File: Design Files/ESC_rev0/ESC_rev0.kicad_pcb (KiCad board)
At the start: 2 copper layers, 176 parts, among them J1 Conn_01x08, J2 Conn_01x06, J3 Conn_01x03, J4 WP-BUTR, J5 WP-BUTR, J6 WP-BUTR, J7 Conn_01x04_Shielded, J8 Conn_01x06, J9 USB_C_Receptacle_USB2.0_16P, Q1 HSBA15810C, Q2 HSBA15810C, Q3 HSBA15810C, Q4 HSBA15810C, Q5 HSBA15810C, Q6 HSBA15810C, SW1 SW_DIP_x01, U1 XT30PW-M, U2 XH-2PWBPZ, U3 AMS1117-3.3, U4 STM32F405RGTx, U5 DRV8302DCA, U6 ESDCAN24-2BLY, U7 SN65HVD230, Y1 Crystal

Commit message: update 14
Circuits separated by schematic pages. Replaced crystal footprint.
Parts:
- Y1: footprint Crystal:Crystal_HC50_Vertical -> Crystal:Crystal_SMD_2012-2Pin_2.0x1.2mm_HandSoldering
- moved H1 104.5 mm to (161.9, 152.8)
- moved H4 104.5 mm to (161.9, 176.7)
- moved R61 104.5 mm to (167.9, 150.1)
- moved R64 104.5 mm to (167.9, 157.6)
- moved H2 104.5 mm to (161.9, 160.8)
- moved R62 104.5 mm to (167.9, 152.6)
- moved R63 104.5 mm to (167.9, 155.1)
- moved H3 104.5 mm to (161.9, 168.7)
- moved D1 104.3 mm to (76.1, 33.3), turned to -90 degrees
- moved U1 98.1 mm to (70.2, 31.0), turned to 90 degrees
- moved C4 87.7 mm to (84.2, 54.5), turned to 180 degrees
- moved C2 84.6 mm to (105.8, 37.1), turned to 90 degrees
- moved C3 83.7 mm to (86.4, 56.1)
- moved R2 83.3 mm to (85.0, 47.4)
- moved R3 83.3 mm to (85.0, 49.9)
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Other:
- board text added: "Analog"
- board text added: "CAN"
- board text added: "Digital"
- board text added: "Filters"
- board text added: "Input Protection"
- board text added: "MCU"
- board text added: "MOSFET Driver"
- board text added: "MOSFETs"
- board text added: "Mechanical"
- board text added: "Power"
- board text added: "Step Down"
- board text added: "USB"

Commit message: update 15
Simple connectors replaced by smd connectors (downloaded). Connectors were placed in edges of the board.
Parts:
- C1, C2: moved to B.Cu
- H1, H2, H3, H4: footprint MountingHole:MountingHole_3.2mm_M3 -> MountingHole:MountingHole_3.2mm_M3_Pad_Via
- J1: footprint Connector_PinHeader_2.00mm:PinHeader_1x08_P2.00mm_Vertical -> HX25003-8AWB:CONN-SMD_8P-P2.50_HX25003-8AWB
- J2, J8: footprint Connector_PinHeader_2.00mm:PinHeader_1x06_P2.00mm_Vertical -> S6B-XH-SM4-TB:CONN_S6B-XH-SM4-TB_JST
- J3: footprint Connector_PinHeader_2.00mm:PinHeader_1x03_P2.00mm_Vertical -> S3B-XH-SM4-TB:CONN3_S3B-XH_JST
- J7: value Conn_01x04_Shielded -> Conn_01x04; footprint Connector_PinHeader_2.00mm:PinHeader_1x04_P2.00mm_Vertical -> S4B-XH-SM4-TB:CONN4_S4B-XH_JST
- U1: value XT30PW-M -> XT60PW-M; footprint Connector_AMASS:AMASS_XT30PW-M_1x02_P2.50mm_Horizontal -> XT60PW-M:XT60PWM
- Y1: footprint Crystal:Crystal_SMD_2012-2Pin_2.0x1.2mm_HandSoldering -> Crystal:Crystal_SMD_0603-4Pin_6.0x3.5mm_HandSoldering
- moved J4 177.7 mm to (220.3, 49.9)
- moved J5 177.7 mm to (220.3, 63.0)
- moved J6 177.7 mm to (220.3, 76.0)
- moved CR1 177.7 mm to (48.0, 44.4)
- moved R54 177.7 mm to (44.1, 33.7)
- moved R55 177.7 mm to (44.1, 36.2)
- moved R56 177.7 mm to (44.1, 38.7)
- moved R57 177.7 mm to (44.1, 41.3)
- moved R58 177.7 mm to (44.1, 43.8)
- moved R59 177.7 mm to (44.1, 46.3)
- moved R60 177.7 mm to (44.1, 48.8)
- moved R33 166.1 mm to (245.0, 108.9)
- moved R34 166.1 mm to (245.0, 111.4)
- moved R35 166.1 mm to (245.0, 113.9)
- moved R36 166.1 mm to (245.0, 116.4)
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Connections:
- J1 pad 1: /MCU/+5V_COM -> GND
- J1 pad 2: /MCU/+3V3_COM -> /MCU/MISO_ADC_EXT2
- J1 pad 3: GND -> /MCU/RX_SCL_MOSI
- J1 pad 4: /MCU/SCK_ADC_EXT -> /MCU/TX_SDA_NSS
- J1 pad 5: /MCU/TX_SDA_NSS -> /MCU/SCK_ADC_EXT
- J1 pad 6: /MCU/RX_SCL_MOSI -> GND
- J1 pad 7: /MCU/MISO_ADC_EXT2 -> /MCU/+3V3_COM
- J1 pad 8: GND -> /MCU/+5V_COM
- U1 pad 1: GND -> +VDC
- U1 pad 2: +VDC -> GND
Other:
- board outline added: 100 x 75 mm
- copper layers 2 -> 4
- board text added: "COM"
- board text added: "Prog"
- board text added: "Sensors"
- board text added: "Servo"
- board text removed: "Mechanical"

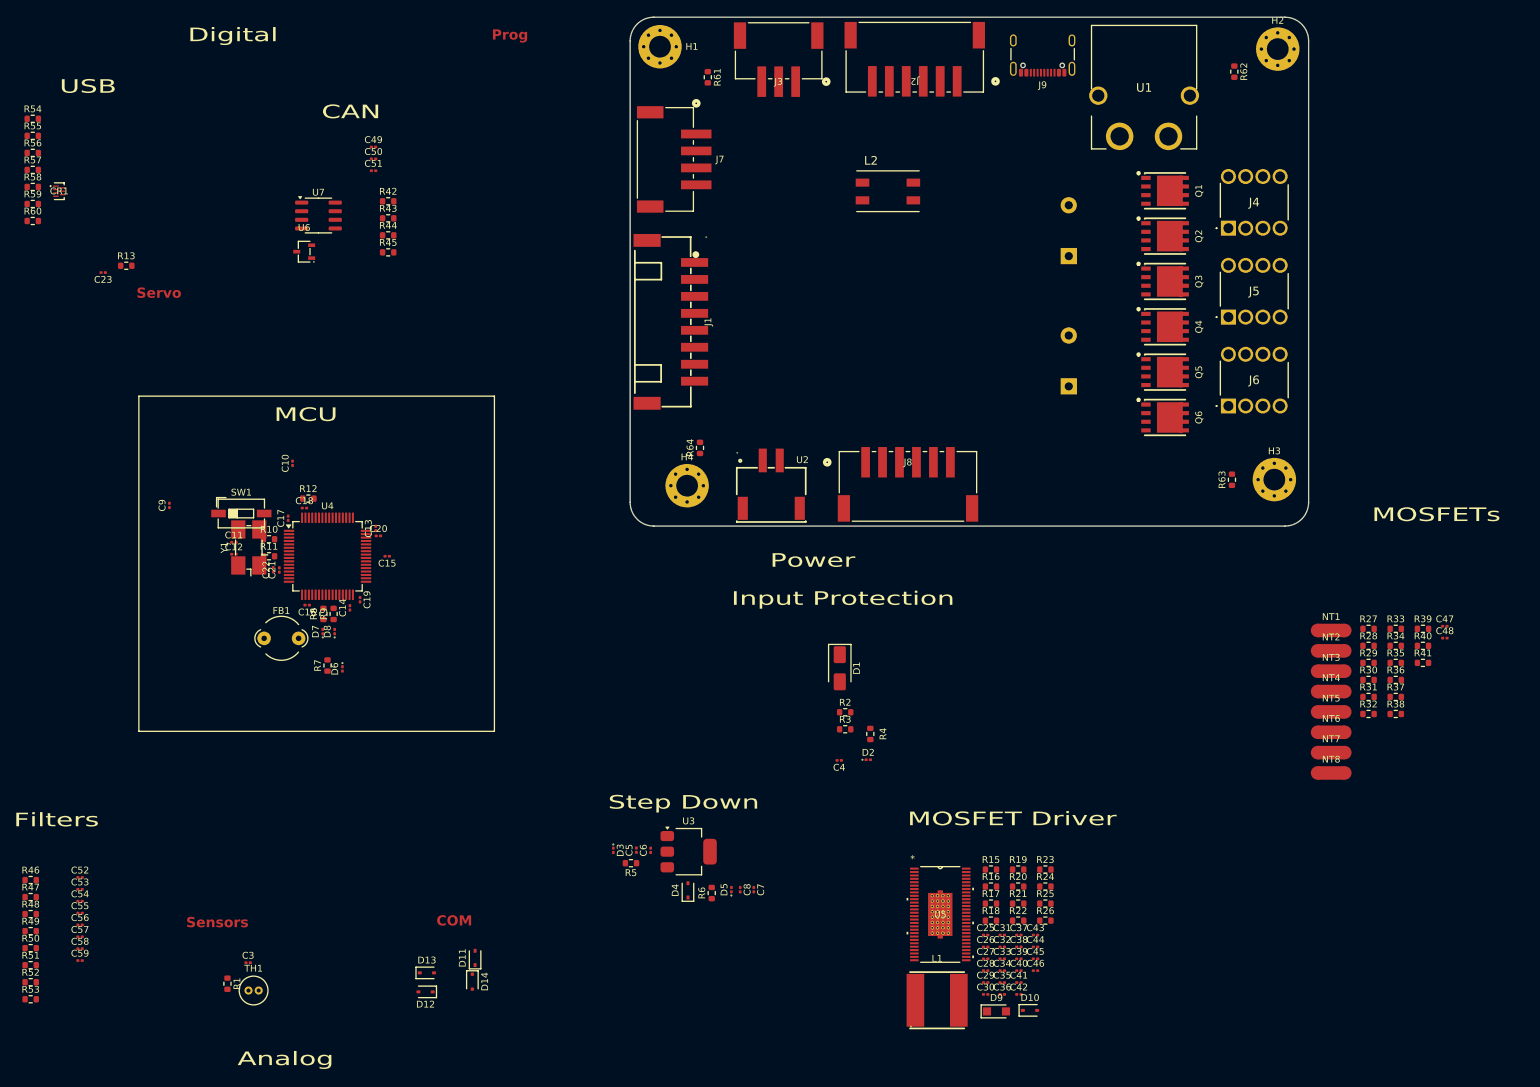
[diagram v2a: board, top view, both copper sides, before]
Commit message: update 16
All components placed on board. Some components modifications and addition were made: added 3D models, changed some symbols and footprints positions and some component types.
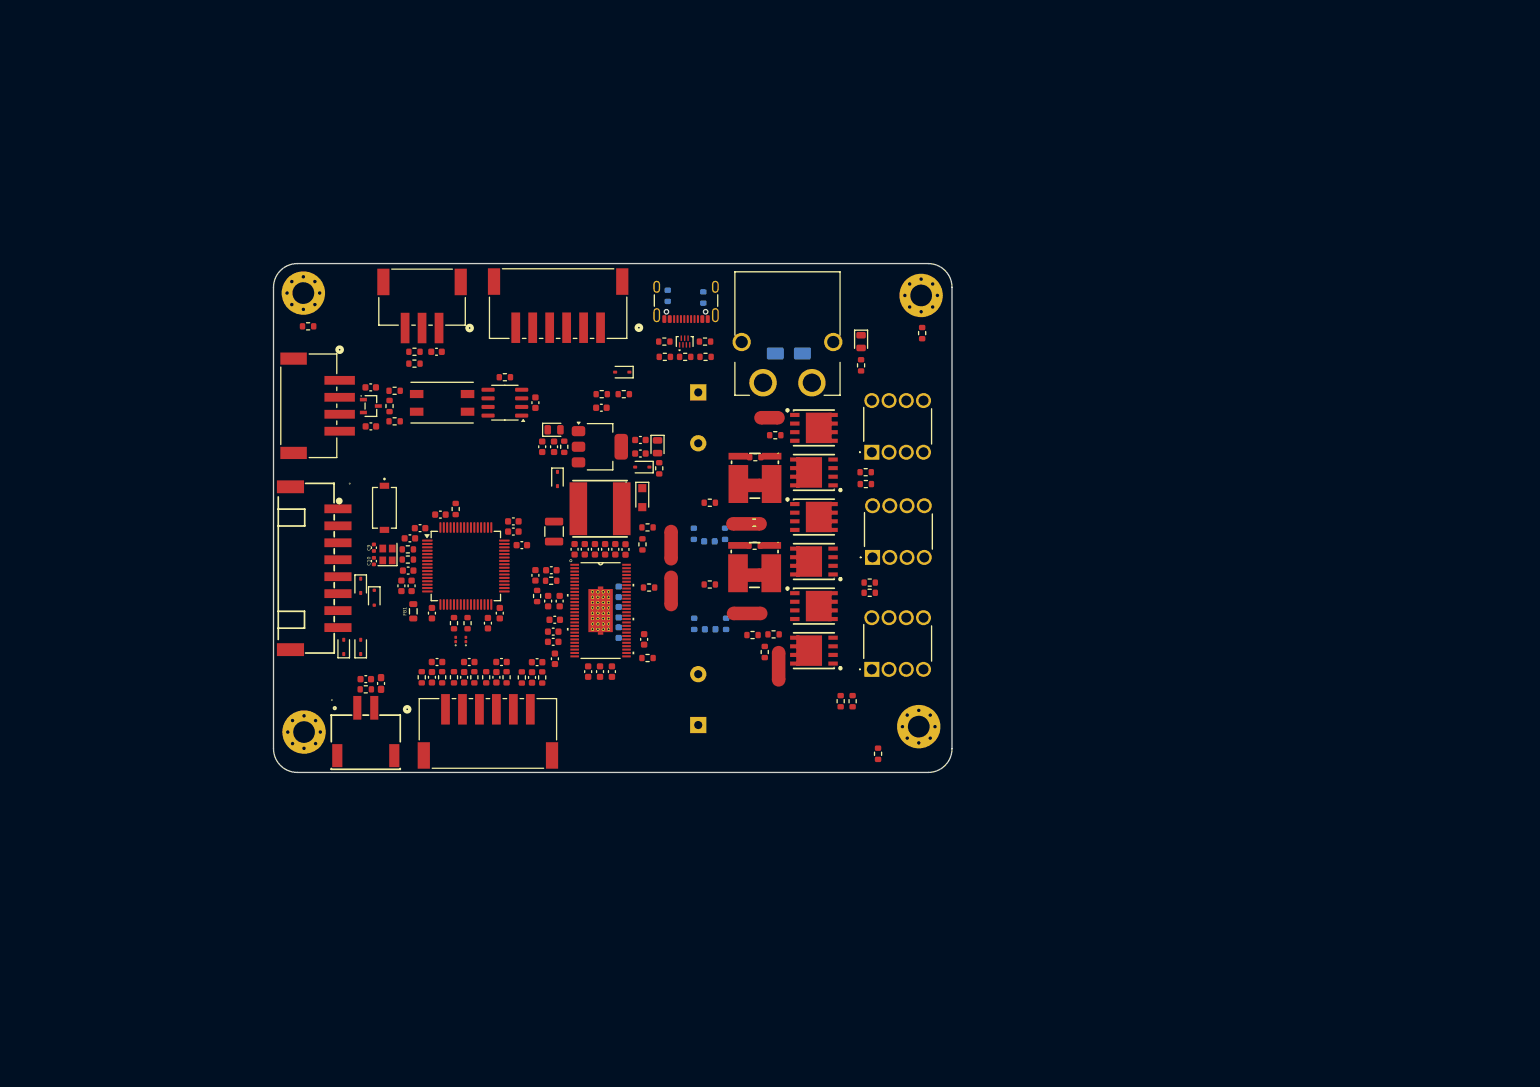
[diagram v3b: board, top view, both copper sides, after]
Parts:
- removed C59: 100n, Capacitor_SMD:C_0201_0603Metric
- removed R63, R64: 0R, Resistor_SMD:R_0603_1608Metric
- added C24: 2u2, Capacitor_SMD:C_0603_1608Metric, F.Cu at (121.8, 104.8)
- added R14: 10k, Resistor_SMD:R_0603_1608Metric, F.Cu at (120.5, 101.8)
- C10: value 100n -> 10p; footprint Capacitor_SMD:C_0201_0603Metric -> Capacitor_SMD:C_0402_1005Metric
- C11: value 10p -> 10u; footprint Capacitor_SMD:C_0201_0603Metric -> Capacitor_SMD:C_0603_1608Metric
- C12: value 10p -> 100n; footprint Capacitor_SMD:C_0201_0603Metric -> Capacitor_SMD:C_0603_1608Metric
- C13, C14, C15, C17, C21, C22, C23, C25, C26, C3, C31, C38, C39, C4, C40, C41, C42, C45, C49, C5, C52, C54, C56, C58, C6, C7, C8: footprint Capacitor_SMD:C_0201_0603Metric -> Capacitor_SMD:C_0603_1608Metric
- C16, C18: value 100n -> 2u2; footprint Capacitor_SMD:C_0201_0603Metric -> Capacitor_SMD:C_0603_1608Metric
- C19, C20: value 2u2 -> 100n; footprint Capacitor_SMD:C_0201_0603Metric -> Capacitor_SMD:C_0603_1608Metric
- C27: value 2u2 -> 6n8; footprint Capacitor_SMD:C_0201_0603Metric -> Capacitor_SMD:C_0603_1608Metric
- C28: value 6n8 -> 2u2; footprint Capacitor_SMD:C_0201_0603Metric -> Capacitor_SMD:C_0603_1608Metric
- C29: value 2u2 -> 120p; footprint Capacitor_SMD:C_0201_0603Metric -> Capacitor_SMD:C_0603_1608Metric
- C30: value 120p -> 2u2; footprint Capacitor_SMD:C_0201_0603Metric -> Capacitor_SMD:C_0603_1608Metric
- C32: value 2u2 -> 220n; footprint Capacitor_SMD:C_0201_0603Metric -> Capacitor_SMD:C_0603_1608Metric; moved to B.Cu
- C33, C34, C47: footprint Capacitor_SMD:C_0201_0603Metric -> Capacitor_SMD:C_0603_1608Metric; moved to B.Cu
- C35: value 220n -> 10uF; footprint Capacitor_SMD:C_0201_0603Metric -> Capacitor_SMD:C_0603_1608Metric
- C36: value 10uF -> 100n; footprint Capacitor_SMD:C_0201_0603Metric -> Capacitor_SMD:C_0603_1608Metric
- C37: value 100n -> 10uF; footprint Capacitor_SMD:C_0201_0603Metric -> Capacitor_SMD:C_0603_1608Metric
- C43: value 10uF -> 100u; footprint Capacitor_SMD:C_0201_0603Metric -> Capacitor_SMD:C_1210_3225Metric
- C44: value 100u -> 10uF; footprint Capacitor_SMD:C_0201_0603Metric -> Capacitor_SMD:C_0603_1608Metric
- C46: value 10uF -> 2n2; footprint Capacitor_SMD:C_0201_0603Metric -> Capacitor_SMD:C_0603_1608Metric; moved to B.Cu
- C48: value 2n2 -> 10p; footprint Capacitor_SMD:C_0201_0603Metric -> Capacitor_SMD:C_0603_1608Metric
- C50: value 10p -> 2u2; footprint Capacitor_SMD:C_0201_0603Metric -> Capacitor_SMD:C_0603_1608Metric
- C51: value 2u2 -> 4n7; footprint Capacitor_SMD:C_0201_0603Metric -> Capacitor_SMD:C_0603_1608Metric
- C53, C57: value 4n7 -> 100n; footprint Capacitor_SMD:C_0201_0603Metric -> Capacitor_SMD:C_0603_1608Metric
- C55: value 100n -> 4n7; footprint Capacitor_SMD:C_0201_0603Metric -> Capacitor_SMD:C_0603_1608Metric
- C9: value 10u -> 10p; footprint Capacitor_SMD:C_0201_0603Metric -> Capacitor_SMD:C_0402_1005Metric
- D1, R53, R54: moved to B.Cu
- D11: value SD05_SOD323 -> LED_R; footprint Diode_SMD:D_SOD-323 -> LED_SMD:LED_0201_0603Metric
- D13: value BAT60A -> PMEG6020AELR; footprint Diode_SMD:D_SOD-323 -> Diode_SMD:Nexperia_CFP3_SOD-123W
- D14: value PESD3V3U1UA -> BAT60A; footprint Diode_SMD:D_SOD-323F -> Diode_SMD:D_SOD-323
- D2, D3, D5: footprint LED_SMD:LED_0201_0603Metric -> LED_SMD:LED_0805_2012Metric
- D6: value LED -> PESD3V3U1UA; footprint LED_SMD:LED_0201_0603Metric -> Diode_SMD:D_SOD-323F
- D7: value LED_G -> BAT60A; footprint LED_SMD:LED_0201_0603Metric -> Diode_SMD:D_SOD-323
- D8: value LED_R -> SD05_SOD323; footprint LED_SMD:LED_0201_0603Metric -> Diode_SMD:D_SOD-323
- D9: value PMEG6020AELR -> LED_G; footprint Diode_SMD:Nexperia_CFP3_SOD-123W -> LED_SMD:LED_0201_0603Metric
- FB1: footprint Ferrite_THT:LairdTech_28C0236-0JW-10 -> Inductor_SMD:L_0805_2012Metric
- NT1, NT2, NT5: footprint NetTie:NetTie-2_SMD_Pad2.0mm -> NetTie:NetTie-2_SMD_Pad2.00mm_Small
- R11: value 0R -> 100R
- R12: value 100R -> 2k2
- R13: value 2k2 -> 16k2
- R15: value 16k2 -> 205k
- R16: value 10k -> 1M
- R17: value 205k -> 10k
- R18: value 1M -> 3k3
- R19: value 10k -> 39k
- R20: value 3k3 -> 2k2
- R25, R31, R37: value 39k -> 4R7
- R26: value 2k2 -> 4R7
- R27, R33: value 4R7 -> 100R
- R28, R34: value 4R7 -> 100R; moved to B.Cu
- R29, R35: value 100R -> 39k; moved to B.Cu
- R30, R36: value 100R -> FKM5R0005FE-TR; footprint Resistor_SMD:R_0603_1608Metric -> FKM5R0005FE-TR:RES-SMD_4P-L6.9-W6.6_OHMITE_FKM5RXXXXFE-TR
- R32, R38: value 0R001_Shunt -> 4R7
- R39: value 4R7 -> 39k
- R40: value 4R7 -> 120R
- R41: value 39k -> 60R
- R42: value 120R -> 60R
- R43: value 60R -> 10k
- R44: value 60R -> 2k2
- R45, R48: value 10k -> 2k2
- R46, R47, R50: value 2k2 -> 10k
- R51, R52: value 10k -> 0R
- R55, R56: value 0R -> 5k1
- R57, R58: value 5k1 -> 22R
- R59, R60: value 22R -> 0R
- R7: value 1K -> 1k
- R9: value 1k -> 0R
- SW1: value SW_DIP_x01 -> Push Button; footprint Button_Switch_SMD:SW_DIP_SPSTx01_Slide_6.7x4.1mm_W6.73mm_P2.54mm_LowProfile_JPin -> Pushbutton 2p:SW_PTS636_SM43J_SMTR_LFS
- TH1: footprint Capacitor_THT:C_Radial_D4.0mm_H5.0mm_P1.50mm -> Capacitor_SMD:C_0603_1608Metric_Pad1.08x0.95mm_HandSolder
- Y1: footprint Crystal:Crystal_SMD_0603-4Pin_6.0x3.5mm_HandSoldering -> Crystal:Crystal_SMD_2520-4Pin_2.5x2.0mm
- moved C48 161.3 mm to (93.9, 79.1), turned to 180 degrees
- moved R41 156.9 mm to (96.7, 76.1), turned to 90 degrees
- moved R53 139.9 mm to (137.7, 59.8), turned to 90 degrees
- moved R62 113.4 mm to (168.7, 127.3)
- moved D10 112.3 mm to (92.4, 111.6), turned to 90 degrees
- moved C47 108.3 mm to (143.9, 109.0)
- moved R34 103.5 mm to (141.6, 108.2), turned to 90 degrees
- moved R57 102.9 mm to (143.3, 68.8), turned to 180 degrees
- moved R37 102.4 mm to (143.9, 102.4)
- moved R54 102.3 mm to (142.9, 60.1), turned to -90 degrees
- moved R58 101.7 mm to (143.2, 66.6)
- moved R55 101.5 mm to (140.3, 68.8)
- moved R31 101.2 mm to (143.9, 90.3)
- moved R28 100.8 mm to (141.5, 94.9), turned to 90 degrees
- moved NT6 99.5 mm to (138.2, 103.3), turned to -90 degrees
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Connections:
- C10 pad 1: +3V3 -> GND
- C10 pad 2: GND -> Net-(C10-Pad2)
- C11 pad 1: GND -> +3V3
- C11 pad 2: Net-(C11-Pad2) -> GND
- C12 pad 1: GND -> /MCU/NRST
- C12 pad 2: Net-(C12-Pad2) -> GND
- C15 pad 1: /MCU/NRST -> +3V3
- C16 pad 1: +3V3 -> /MCU/VCAP_1
- C18 pad 1: +3V3 -> /MCU/VCAP_2
- C19 pad 1: /MCU/VCAP_1 -> +3V3
- C20 pad 1: /MCU/VCAP_2 -> +3V3
- C26 pad 1: /MOSFET DRIVER/DVDD -> Net-(U5-GVDD)
- C27 pad 1: Net-(U5-GVDD) -> GND
- C27 pad 2: GND -> Net-(C27-Pad2)
- C28 pad 1: GND -> Net-(U5-GVDD)
- C28 pad 2: Net-(C28-Pad2) -> GND
- C29 pad 1: Net-(U5-GVDD) -> GND
- C29 pad 2: GND -> Net-(U5-COMP)
- C30 pad 1: GND -> Net-(U5-AVDD)
- C30 pad 2: Net-(U5-COMP) -> GND
- C31 pad 1: Net-(U5-AVDD) -> Net-(U5-CP1)
- C31 pad 2: GND -> Net-(U5-CP2)
- C32 pad 1: Net-(U5-CP1) -> /MOSFET DRIVER/BST1
- C32 pad 2: Net-(U5-CP2) -> SH1
- C33 pad 1: /MOSFET DRIVER/BST1 -> /MOSFET DRIVER/BST2
- C33 pad 2: SH1 -> SH2
- C34 pad 1: /MOSFET DRIVER/BST2 -> /MOSFET DRIVER/BST3
- C34 pad 2: SH2 -> SH3
- C35 pad 1: /MOSFET DRIVER/BST3 -> +VDC
- C35 pad 2: SH3 -> GND
- C36 pad 1: +VDC -> Net-(U5-BST_BK)
- C36 pad 2: GND -> /MOSFET DRIVER/PH
- C37 pad 1: Net-(U5-BST_BK) -> +VDC
- C37 pad 2: /MOSFET DRIVER/PH -> GND
- C38 pad 2: GND -> Net-(C38-Pad2)
- C39 pad 2: Net-(C39-Pad2) -> GND
- C40 pad 2: GND -> Net-(C38-Pad2)
- C41 pad 2: Net-(C39-Pad2) -> Net-(C38-Pad2)
- C42 pad 2: Net-(C39-Pad2) -> Net-(C38-Pad2)
- C43 pad 1: +VDC -> /MOSFET DRIVER/+5V_x
- C43 pad 2: Net-(C39-Pad2) -> GND
- C44 pad 1: /MOSFET DRIVER/+5V_x -> +VDC
- C44 pad 2: GND -> Net-(C38-Pad2)
- C45 pad 2: Net-(C39-Pad2) -> Net-(C38-Pad2)
- C46 pad 1: +VDC -> SN1
- C46 pad 2: Net-(C39-Pad2) -> SP1
- C47 pad 1: SN1 -> SN2
- C47 pad 2: SP1 -> SP2
- C48 pad 1: SN2 -> GND
- C48 pad 2: SP2 -> /CAN/C_CAN_P
- C49 pad 1: GND -> /CAN/C_CAN_N
- C49 pad 2: /CAN/C_CAN_P -> GND
- C50 pad 1: /CAN/C_CAN_N -> +3V3
- C51 pad 1: +3V3 -> /Filters/HALL_1_IN
- C52 pad 1: /Filters/HALL_1_IN -> /Filters/HALL_3_IN
- C53 pad 1: /Filters/HALL_3_IN -> +3.3V
- C55 pad 1: +3.3V -> /Filters/HALL_2_IN
- C56 pad 1: /Filters/HALL_2_IN -> /Filters/TEMP_IN
- C57 pad 1: /Filters/TEMP_IN -> +3.3V
- C9 pad 1: +3V3 -> GND
- C9 pad 2: GND -> Net-(C9-Pad2)
- D10 pad 2: /MOSFET DRIVER/+5V_x -> /MCU/+5V_COM
- D11 pad 2: /MCU/+5V_COM -> Net-(D11-A)
- D12 pad 1: +5V -> +3V3
- D12 pad 2: /MCU/+5V_COM -> /MCU/+3V3_DBG
- D13 pad 1: +3V3 -> /MOSFET DRIVER/PH
- D13 pad 2: /MCU/+3V3_COM -> GND
- D14 pad 1: /MCU/+3V3_COM -> +5V
- D14 pad 2: GND -> /MOSFET DRIVER/+5V_x
- D6 pad 1: GND -> /MCU/+3V3_COM
- D6 pad 2: Net-(D6-A) -> GND
- D7 pad 1: GND -> +3V3
- D7 pad 2: Net-(D7-A) -> /MCU/+3V3_COM
- D8 pad 2: Net-(D8-A) -> /MCU/+5V_COM
- D9 pad 1: /MOSFET DRIVER/PH -> GND
- D9 pad 2: GND -> Net-(D9-A)
- J2 pad 1: +3V3 -> /MCU/+3V3_DBG
- L2 pad 1: /CAN/R_CAN_P -> /CAN/R_CAN_N
- L2 pad 2: /CAN/R_CAN_N -> /CAN/R_CAN_P
- L2 pad 3: /CAN/CAN_N -> /CAN/CAN_P
- L2 pad 4: /CAN/CAN_P -> /CAN/CAN_N
- R10 pad 1: Net-(C11-Pad2) -> Net-(C10-Pad2)
- R10 pad 2: /MCU/PH_0_P -> /MCU/PH_1_P
- R11 pad 1: Net-(C12-Pad2) -> +3V3
- R11 pad 2: /MCU/PH_1_P -> /MCU/BOOT0_P
- R12 pad 1: +3V3 -> /MCU/SERVO
- R12 pad 2: /MCU/BOOT0_P -> Net-(J3-Pad3)
- R13 pad 1: /MCU/SERVO -> Net-(C27-Pad2)
- R13 pad 2: Net-(J3-Pad3) -> Net-(U5-COMP)
- R15 pad 1: Net-(C28-Pad2) -> GND
- R15 pad 2: Net-(U5-COMP) -> Net-(U5-RT_CLK)
- R16 pad 1: GND -> /MOSFET DRIVER/BIAS
- R16 pad 2: Net-(U5-DTC) -> GND
- R17 pad 1: GND -> /MOSFET DRIVER/+5V_x
- R17 pad 2: Net-(U5-RT_CLK) -> /MOSFET DRIVER/VSENSE
- R18 pad 1: /MOSFET DRIVER/BIAS -> /MOSFET DRIVER/VSENSE
- R19 pad 1: /MOSFET DRIVER/+5V_x -> SL3
- R19 pad 2: /MOSFET DRIVER/VSENSE -> SENS3
- R20 pad 1: /MOSFET DRIVER/VSENSE -> SENS3
- R21 pad 1: SL3 -> SL2
- R21 pad 2: SENS3 -> SENS2
- R22 pad 1: SENS3 -> SENS2
- R23 pad 1: SL2 -> SL1
- R23 pad 2: SENS2 -> SENS1
- R24 pad 1: SENS2 -> SENS1
- R25 pad 1: SL1 -> GH1
- R25 pad 2: SENS1 -> /MOSFETs/GH1_RG
- R26 pad 1: SENS1 -> GL1
- R26 pad 2: GND -> /MOSFETs/GL1_RG
- R27 pad 1: M_H1 -> SN1
- R27 pad 2: /MOSFETs/GH1_RG -> /MOSFETs/S1_P
- R28 pad 1: M_L1 -> SP1
- R28 pad 2: /MOSFETs/GL1_RG -> /MOSFETs/S1_N
- R29 pad 1: SN1 -> /MOSFETs/GL1_RG
- R29 pad 2: /MOSFETs/S1_P -> GND
- R30 pad 1: SP1 -> Net-(NT3-Pad2)
- R30 pad 2: /MOSFETs/S1_N -> Net-(NT2-Pad1)
- R31 pad 1: /MOSFETs/GL1_RG -> GH2
- R31 pad 2: GND -> /MOSFETs/GH2_RG
- R32 pad 1: Net-(NT3-Pad2) -> GL2
- R32 pad 2: /MOSFETs/S1_N -> /MOSFETs/GL2_RG
- R33 pad 1: M_H2 -> SN2
- R33 pad 2: /MOSFETs/GH2_RG -> /MOSFETs/S2_P
- R34 pad 1: M_L2 -> SP2
- R34 pad 2: /MOSFETs/GL2_RG -> /MOSFETs/S2_N
- R35 pad 1: SN2 -> /MOSFETs/GL2_RG
- R35 pad 2: /MOSFETs/S2_P -> GND
- R36 pad 1: SP2 -> Net-(NT6-Pad2)
- R36 pad 2: /MOSFETs/S2_N -> Net-(NT5-Pad1)
- R37 pad 1: /MOSFETs/GL2_RG -> GH3
- R37 pad 2: GND -> /MOSFETs/GH3_RG
- R38 pad 1: Net-(NT6-Pad2) -> GL3
- R38 pad 2: /MOSFETs/S2_N -> /MOSFETs/GL3_RG
- R39 pad 1: M_H3 -> /MOSFETs/GL3_RG
- R39 pad 2: /MOSFETs/GH3_RG -> GND
- R40 pad 1: M_L3 -> /CAN/C_CAN_P
- R40 pad 2: /MOSFETs/GL3_RG -> /CAN/C_CAN_N
- R41 pad 1: /MOSFETs/GL3_RG -> /CAN/C_CAN_P
- R41 pad 2: GND -> /CAN/R_CAN_P
- R42 pad 1: /CAN/C_CAN_P -> /CAN/C_CAN_N
- R42 pad 2: /CAN/C_CAN_N -> /CAN/R_CAN_N
- R43 pad 1: /CAN/C_CAN_P -> Net-(U7-Rs)
- R43 pad 2: /CAN/R_CAN_P -> GND
- R44 pad 1: /CAN/C_CAN_N -> +3.3V
- R44 pad 2: /CAN/R_CAN_N -> /Filters/HALL_1_IN
- R45 pad 1: Net-(U7-Rs) -> +3.3V
- R45 pad 2: GND -> /Filters/HALL_3_IN
- R46 pad 1: +3.3V -> /Filters/HALL_1_IN
- R46 pad 2: /Filters/HALL_1_IN -> HALL_1_OUT
- R47 pad 1: +3.3V -> /Filters/HALL_3_IN
- R47 pad 2: /Filters/HALL_3_IN -> HALL_3_OUT
- R48 pad 1: /Filters/HALL_1_IN -> +3.3V
- R48 pad 2: HALL_1_OUT -> /Filters/HALL_2_IN
- R49 pad 1: /Filters/HALL_3_IN -> +3.3V
- R49 pad 2: HALL_3_OUT -> /Filters/TEMP_IN
- R50 pad 1: +3.3V -> /Filters/HALL_2_IN
- R50 pad 2: /Filters/HALL_2_IN -> HALL_2_OUT
- R51 pad 1: +3.3V -> /Filters/TEMP_IN
- R51 pad 2: /Filters/TEMP_IN -> TEMP_OUT
- R52 pad 1: /Filters/HALL_2_IN -> Net-(J9-SHIELD)
- R52 pad 2: HALL_2_OUT -> GND
- R53 pad 1: /Filters/TEMP_IN -> Net-(J9-SHIELD)
- R53 pad 2: TEMP_OUT -> GND
- R54 pad 1: Net-(J9-SHIELD) -> +5V
- R54 pad 2: GND -> /USB/+5V-C
- R55 pad 1: Net-(J9-SHIELD) -> /USB/CC2
- R56 pad 1: +5V -> /USB/CC1
- R56 pad 2: /USB/+5V-C -> GND
- R57 pad 1: /USB/CC2 -> /USB/USB-C_N
- R57 pad 2: GND -> USB_N
- R58 pad 1: /USB/CC1 -> /USB/USB-C_P
- R58 pad 2: GND -> USB_P
- R59 pad 1: /USB/USB-C_N -> Net-(H1-Pad1)
- R59 pad 2: USB_N -> GND
- R60 pad 1: /USB/USB-C_P -> Net-(H2-Pad1)
- R60 pad 2: USB_P -> GND
- R61 pad 1: Net-(H1-Pad1) -> Net-(H3-Pad1)
- R62 pad 1: Net-(H2-Pad1) -> Net-(H4-Pad1)
- R7 pad 1: Net-(D6-A) -> Net-(D9-A)
- R7 pad 2: +3V3 -> /MCU/LED_GREEN
- R8 pad 1: Net-(D7-A) -> Net-(D11-A)
- R8 pad 2: /MCU/LED_GREEN -> /MCU/LED_RED
- R9 pad 1: Net-(D8-A) -> Net-(C9-Pad2)
- R9 pad 2: /MCU/LED_RED -> /MCU/PH_0_P
- U4 pad 44: /MCU/USB_DM -> USB_N
- U4 pad 45: /MCU/USB_DP -> USB_P
- U4 pad 8: /MCU/TEMP_MOTOR -> TEMP_OUT
- U6 pad 1: /CAN/C_CAN_P -> /CAN/C_CAN_N
- U6 pad 2: /CAN/C_CAN_N -> /CAN/C_CAN_P
- Y1 pad 1: Net-(C12-Pad2) -> Net-(C10-Pad2)
- Y1 pad 2: Net-(C11-Pad2) -> Net-(C9-Pad2)
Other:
- board text removed: "Analog"
- board text removed: "CAN"
- board text removed: "COM"
- board text removed: "Digital"
- board text removed: "Filters"
- board text removed: "Input Protection"
- board text removed: "MCU"
- board text removed: "MOSFET Driver"
- board text removed: "MOSFETs"
- board text removed: "Power"
- board text removed: "Prog"
- board text removed: "Sensors"
- board text removed: "Servo"
- board text removed: "Step Down"
- board text removed: "USB"

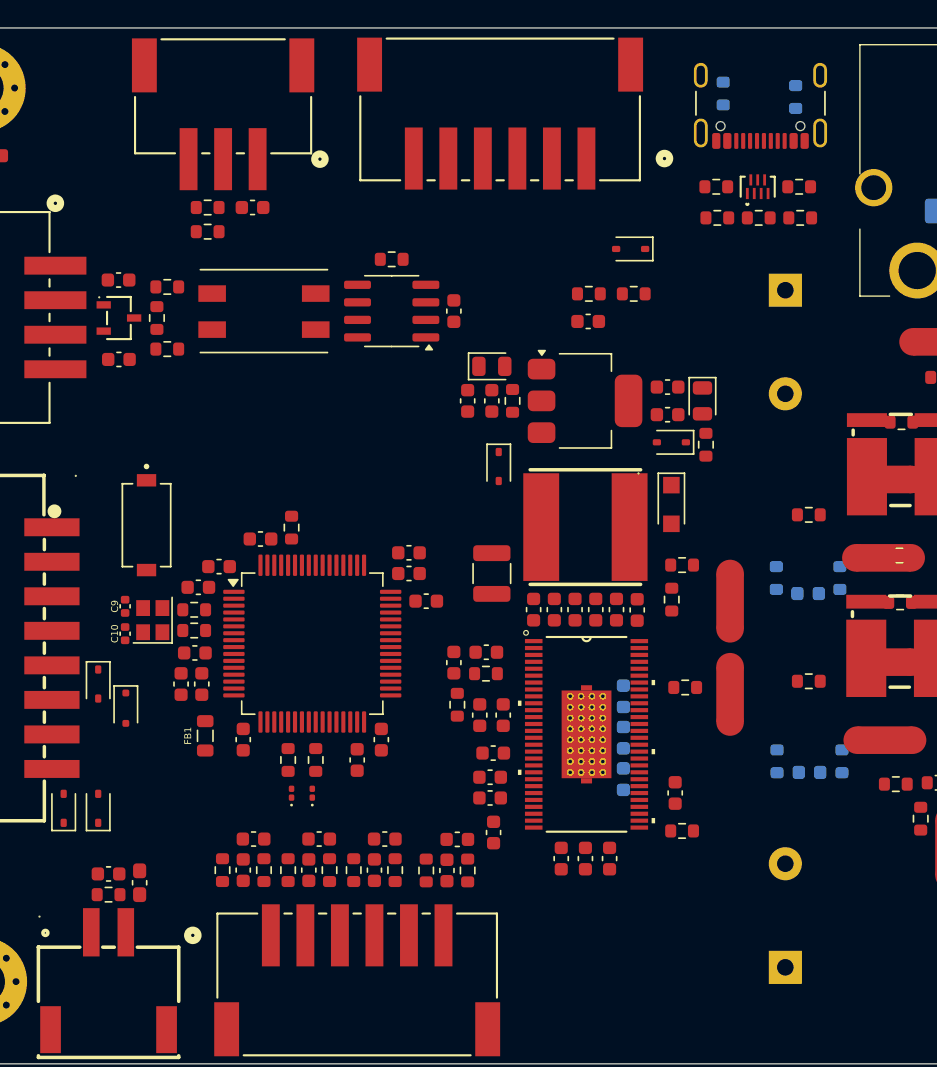
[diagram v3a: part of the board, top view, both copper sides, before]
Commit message: update 17
Defined board stackup, constraints and net classes for USB and CAN. Some components were slightly moved; shunt filters were place next do the gate driver pins. External calculators were used, check course documentation.
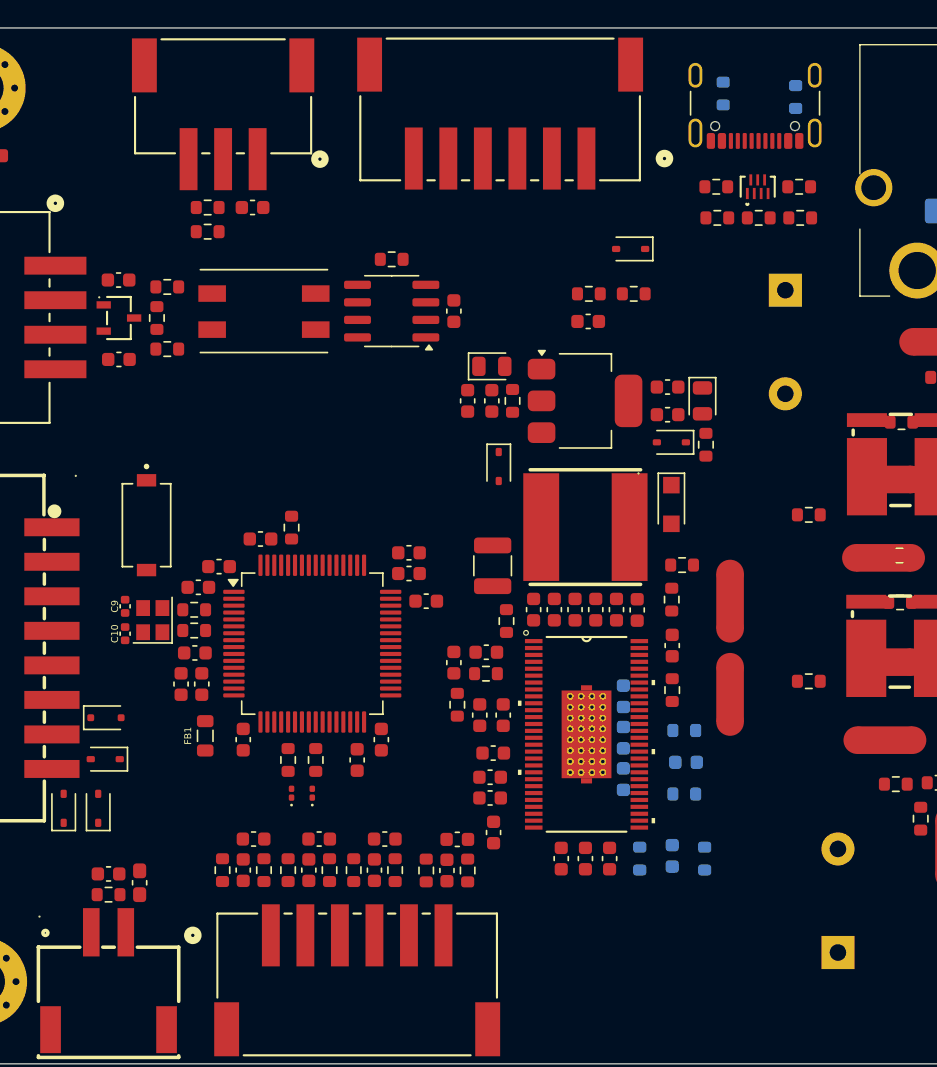
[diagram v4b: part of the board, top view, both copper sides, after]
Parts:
- moved R17 19.8 mm to (122.0, 98.0), turned to -90 degrees
- moved R28 17.0 mm to (134.9, 110.5), turned to 180 degrees
- moved R29 15.8 mm to (134.9, 105.9), turned to 180 degrees
- moved C46 15.1 mm to (135.0, 108.2), turned to 0 degrees
- moved R35 12.2 mm to (136.3, 115.2), turned to -90 degrees
- moved R34 12.2 mm to (131.7, 115.2)
- moved C47 11.6 mm to (134.0, 115.0), turned to -90 degrees
- moved C36 10.7 mm to (134.0, 99.8)
- moved D7 5.46 mm to (93.0, 108.0), turned to 180 degrees
- moved C1 3.96 mm to (146.0, 122.0)
- moved D6 1.60 mm to (93.0, 105.0), turned to 0 degrees
- moved R16 0.96 mm to (134.0, 103.0), turned to -90 degrees
- moved C43 0.56 mm to (121.0, 94.0), turned to 90 degrees
- moved J9 0.39 mm to (140.0, 59.6)
